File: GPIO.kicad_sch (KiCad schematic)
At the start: 0 parts

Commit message: Adde the sub sheet schematic for the GPIO and connected the Hierchal sheets together
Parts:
- added J10, J11, J14, J8: Conn_01x03_Pin, A_HDJ_Library:PinHeader_1x03_P2.54mm_Vertical, symbol Connector:Conn_01x03_Pin
- added J12, J13, J15, J16, J19, J7, J9: Conn_01x04_Pin, A_HDJ_Library:PinHeader_1x04_P2.54mm_Vertical, symbol Connector:Conn_01x04_Pin
- added U10, U11, U12, U17, U9: D3V3XA4B10LP, A_HDJ_Library:Diodes_UDFN-10_1.0x2.5mm_P0.5mm, symbol Power_Protection:D3V3XA4B10LP
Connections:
- new net: U17.3 (VSS), U17.8 (VSS)
- new net: U12.5, U12.6 (NC)
- new net: U10.5, U10.6 (NC)
- new net +3.3V: J13.1 (Pin_1), J13.2 (Pin_2), J13.3 (Pin_3), J13.4 (Pin_4), J14.1 (Pin_1), J14.2 (Pin_2), J14.3 (Pin_3), J19.1 (Pin_1), J19.2 (Pin_2), J19.3 (Pin_3), J19.4 (Pin_4)
- new net GND: J11.1 (Pin_1), J11.2 (Pin_2), J11.3 (Pin_3), J12.1 (Pin_1), J12.2 (Pin_2), J12.3 (Pin_3), J12.4 (Pin_4), J16.1 (Pin_1), J16.2 (Pin_2), J16.3 (Pin_3), J16.4 (Pin_4), U10.3 (VSS), U10.8 (VSS), U11.3 (VSS), U11.8 (VSS), U12.3 (VSS), U12.8 (VSS), U9.3 (VSS), U9.8 (VSS)
- new net GPP_D0: J15.1 (Pin_1), U17.1, U17.10 (NC)
- new net GPP_D1: J15.2 (Pin_2), U17.2, U17.9 (NC)
- new net GPP_D2: J15.3 (Pin_3), U17.4, U17.7 (NC)
- new net GPP_D3: J15.4 (Pin_4), U17.5, U17.6 (NC)
- new net I2C2_SCL: J9.1 (Pin_1), U11.1, U11.10 (NC)
- new net I2C2_SDA: J7.1 (Pin_1), U9.1, U9.10 (NC)
- new net I2C3_SCL: J9.2 (Pin_2), U11.2, U11.9 (NC)
- new net I2C3_SDA: J7.2 (Pin_2), U9.2, U9.9 (NC)
- new net I2C4_SCL: J9.3 (Pin_3), U11.4, U11.7 (NC)
- new net I2C4_SDA: J7.3 (Pin_3), U9.4, U9.7 (NC)
- new net I2C5_SCL: J9.4 (Pin_4), U11.5, U11.6 (NC)
- new net I2C5_SDA: J7.4 (Pin_4), U9.5, U9.6 (NC)
- new net SOC_UART0_RX: J8.1 (Pin_1), U10.1, U10.10 (NC)
- new net SOC_UART0_TX: J10.1 (Pin_1), U12.1, U12.10 (NC)
- new net SOC_UART1_RX: J8.2 (Pin_2), U10.2, U10.9 (NC)
- new net SOC_UART1_TX: J10.2 (Pin_2), U12.2, U12.9 (NC)
- new net SOC_UART2_RX: J8.3 (Pin_3), U10.4, U10.7 (NC)
- new net SOC_UART2_TX: J10.3 (Pin_3), U12.4, U12.7 (NC)

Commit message: finished the pciex4 implememntation
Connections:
- net GND: now also U17.3 (VSS), U17.8 (VSS)
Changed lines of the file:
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@@
+		)
+	)
+	(symbol
+		(lib_id "power:GND")
+		(at 243.84 87.63 0)
+		(unit 1)
+		(body_style 1)
+		(exclude_from_sim no)
+		(in_bom yes)
+		(on_board yes)
+		(in_pos_files yes)
+		(dnp no)
+		(fields_autoplaced yes)
+		(property "Reference" "#PWR0144"
+			(at 243.84 93.98 0)
+			(hide yes)
+			(show_name no)
+			(do_not_autoplace no)
+			(effects
+				(font
+					(size 1.27 1.27)
+				)
+			)
+		)
+		(property "Value" "GND"
+			(at 243.84 92.71 0)
+			(show_name no)
+			(do_not_autoplace no)
+			(effects
+				(font
+					(size 1.27 1.27)
+				)
+			)
+		)
+		(property "Footprint" ""
+			(at 243.84 87.63 0)
+			(hide yes)
+			(show_name no)
+			(do_not_autoplace no)
+			(effects
+				(font
+					(size 1.27 1.27)
+				)
+			)
+		)
+		(property "Datasheet" ""
+			(at 243.84 87.63 0)
+			(hide yes)
+			(show_name no)
+			(do_not_autoplace no)
+			(effects
+				(font
+					(size 1.27 1.27)
+				)
+			)
+		)
+		(property "Description" "Power symbol creates a global label with name \"GND\" , ground"
+			(at 243.84 87.63 0)
+			(hide yes)
+			(show_name no)
+			(do_not_autoplace no)
+			(effects
+				(font
+					(size 1.27 1.27)
+				)
+			)
+		)
+		(pin "1"
+		)
+		(instances
+			(project "Carrier_Board"
+				(path "/e768274e-12f3-4f83-96f6-abb7638e0bc1/f0c5bd9b-b5d7-485d-b3b5-c60eebcf14e3"
+					(reference "#PWR0144")
+					(unit 1)
+				)
+			)
 		)
 	)

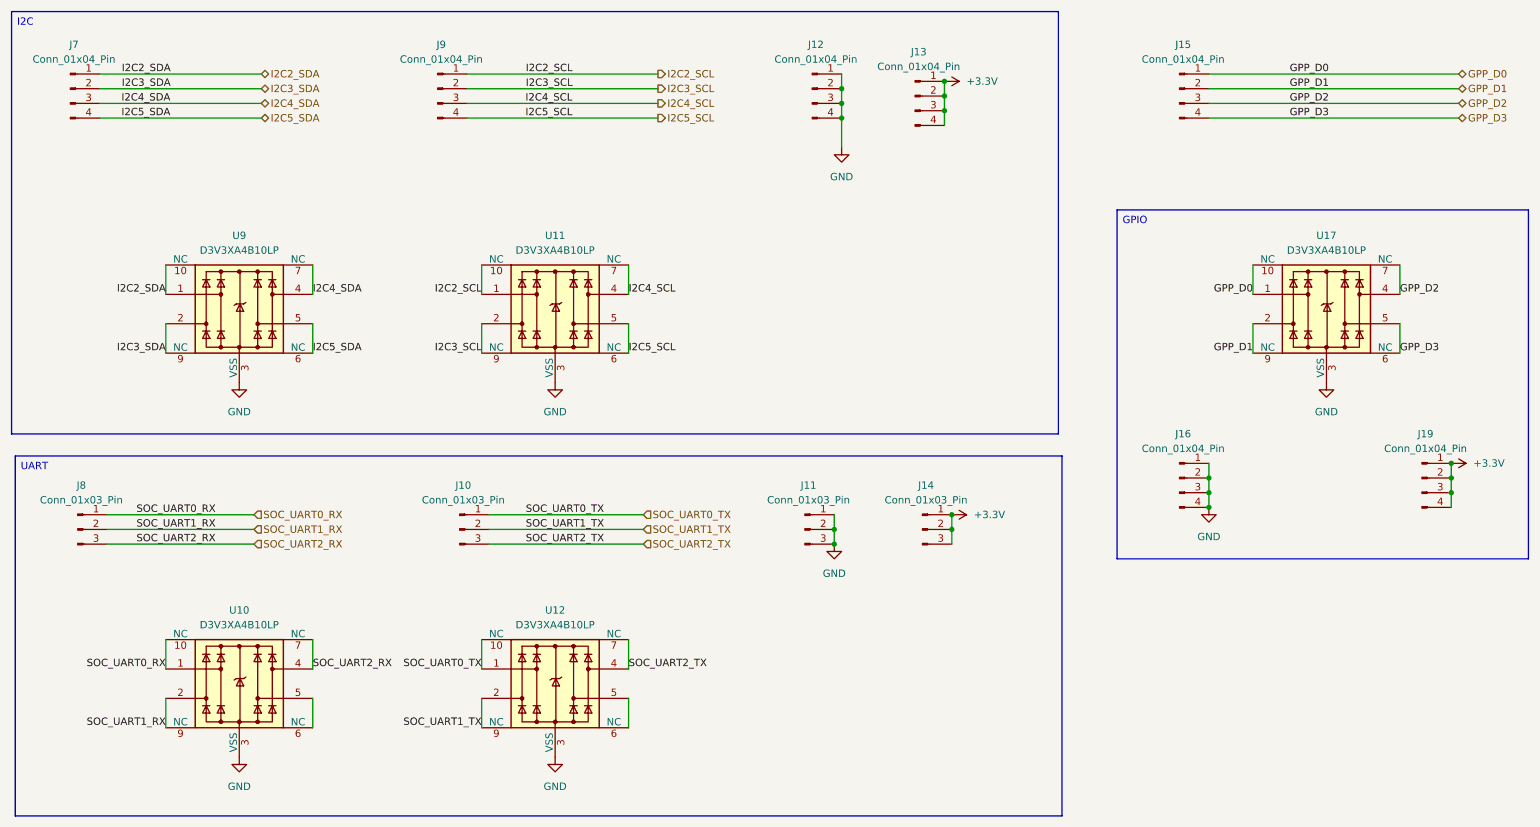
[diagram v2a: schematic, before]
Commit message: Fixed annotation errors duplicate designators on passive components R11 and J15 so that schematic could be imported into pcb. There might be some missing footprints... starting that investigation
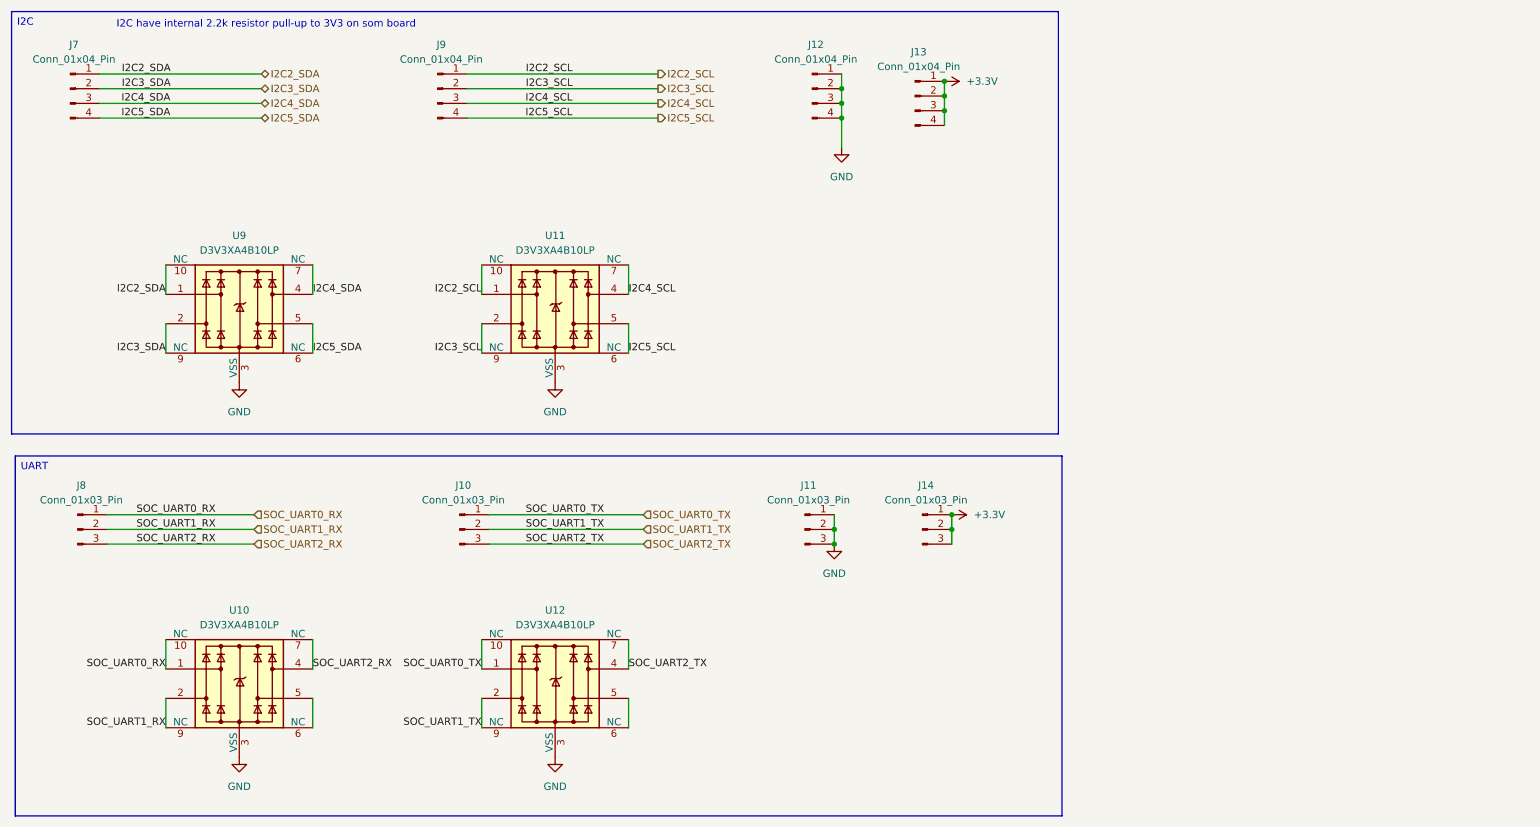
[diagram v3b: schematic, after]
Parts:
- removed J15, J16, J19: Conn_01x04_Pin, A_HDJ_Library:PinHeader_1x04_P2.54mm_Vertical, symbol Connector:Conn_01x04_Pin
- removed U17: D3V3XA4B10LP, A_HDJ_Library:Diodes_UDFN-10_1.0x2.5mm_P0.5mm, symbol Power_Protection:D3V3XA4B10LP
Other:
- note added: "I2C have internal 2.2k resistor pull-up to 3V3 on som board"

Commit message: Updated all the footprints into the pcb editor but all the designator numbers have changed... I have tp go back and fix each one
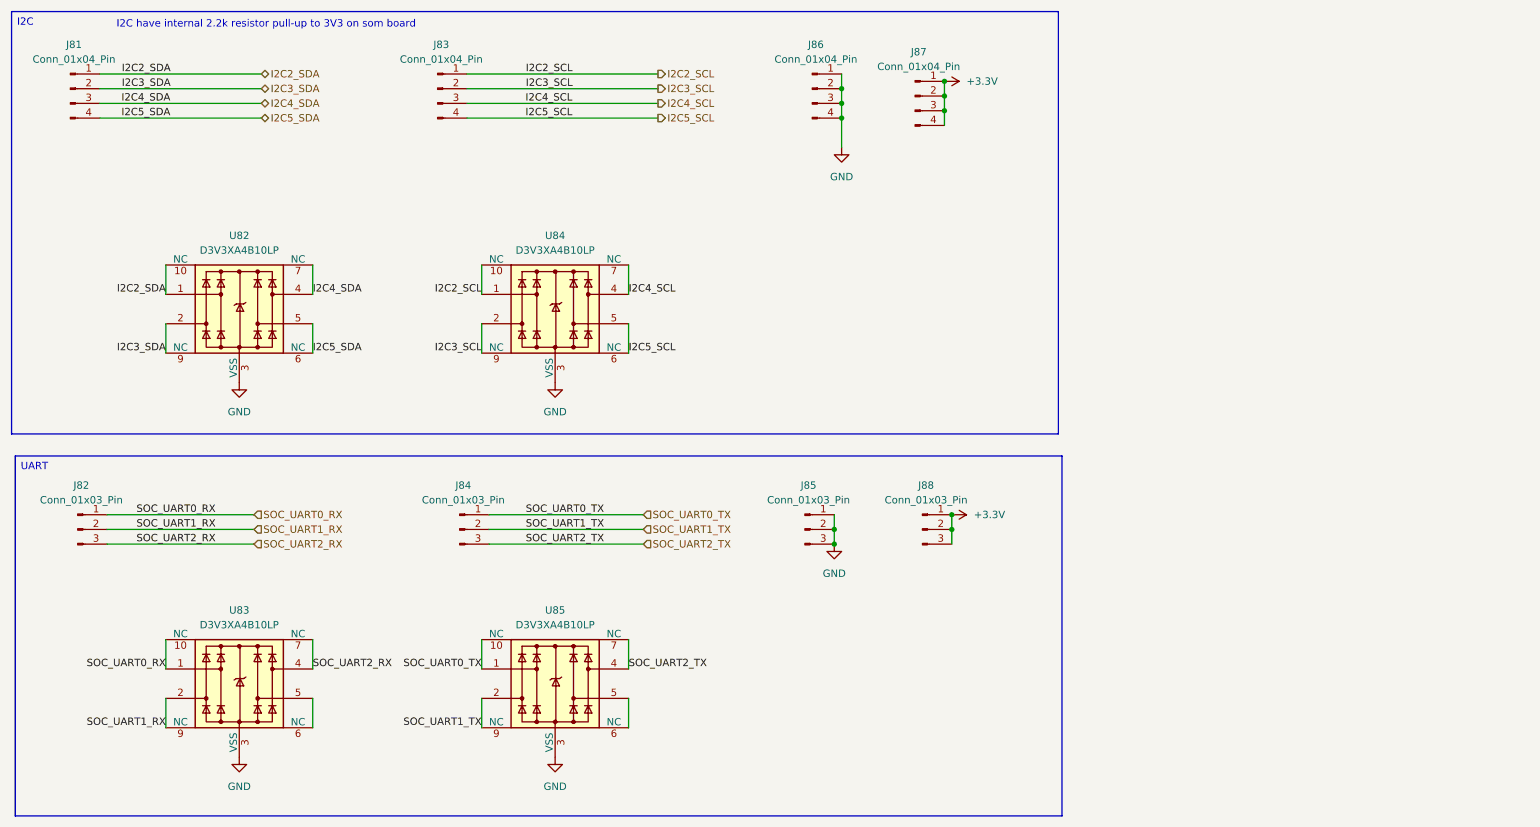
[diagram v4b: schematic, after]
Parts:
- renumbered J7 to J81, J8 to J82, J9 to J83, J10 to J84, J11 to J85, J12 to J86, J13 to J87, J14 to J88, U9 to U82, U10 to U83, U11 to U84, U12 to U85

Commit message: Designators in GPIO restored
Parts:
- renumbered J84 to J10, J85 to J11, J86 to J12, J87 to J13, J88 to J14, J81 to J7, J82 to J8, J83 to J9, U83 to U10, U84 to U11, U85 to U12, U82 to U9
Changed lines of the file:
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@@
 		(dnp no)
 		(fields_autoplaced yes)
-		(property "Reference" "J83"
+		(property "Reference" "J9"
 			(at 90.805 29.21 0)
 			(show_name no)
@@
 			(project "Carrier_Board"
 				(path "/e768274e-12f3-4f83-96f6-abb7638e0bc1/f0c5bd9b-b5d7-485d-b3b5-c60eebcf14e3"
-					(reference "J83")
+					(reference "J9")
 					(unit 1)
 				)
@@
 		(dnp no)
 		(fields_autoplaced yes)
-		(property "Reference" "J84"
+		(property "Reference" "J10"
 			(at 94.615 105.41 0)
 			(show_name no)
@@
 			(project "Carrier_Board"
 				(path "/e768274e-12f3-4f83-96f6-abb7638e0bc1/f0c5bd9b-b5d7-485d-b3b5-c60eebcf14e3"
-					(reference "J84")
+					(reference "J10")
 					(unit 1)
 				)
@@
 		(dnp no)
 		(fields_autoplaced yes)
-		(property "Reference" "U85"
+		(property "Reference" "U12"
 			(at 110.49 127 0)
 			(show_name no)
@@
 			(project "Carrier_Board"
 				(path "/e768274e-12f3-4f83-96f6-abb7638e0bc1/f0c5bd9b-b5d7-485d-b3b5-c60eebcf14e3"
-					(reference "U85")
+					(reference "U12")
 					(unit 1)
 				)
@@
 		(dnp no)
 		(fields_autoplaced yes)
-		(property "Reference" "U83"
+		(property "Reference" "U10"
 			(at 55.88 127 0)
 			(show_name no)
@@
 			(project "Carrier_Board"
 				(path "/e768274e-12f3-4f83-96f6-abb7638e0bc1/f0c5bd9b-b5d7-485d-b3b5-c60eebcf14e3"
-					(reference "U83")
+					(reference "U10")
 					(unit 1)
 				)
@@
 		(dnp no)
 		(fields_autoplaced yes)
-		(property "Reference" "U84"
+		(property "Reference" "U11"
 			(at 110.49 62.23 0)
 			(show_name no)
@@
 			(project "Carrier_Board"
 				(path "/e768274e-12f3-4f83-96f6-abb7638e0bc1/f0c5bd9b-b5d7-485d-b3b5-c60eebcf14e3"
-					(reference "U84")
+					(reference "U11")
 					(unit 1)
 				)
@@
 		(dnp no)
 		(fields_autoplaced yes)
-		(property "Reference" "J85"
+		(property "Reference" "J11"
 			(at 154.305 105.41 0)
 			(show_name no)
@@
 			(project "Carrier_Board"
 				(path "/e768274e-12f3-4f83-96f6-abb7638e0bc1/f0c5bd9b-b5d7-485d-b3b5-c60eebcf14e3"
-					(reference "J85")
+					(reference "J11")
 					(unit 1)
 				)
@@
 		(dnp no)
 		(fields_autoplaced yes)
-		(property "Reference" "J81"
+		(property "Reference" "J7"
 			(at 27.305 29.21 0)
 			(show_name no)
@@
 			(project "Carrier_Board"
 				(path "/e768274e-12f3-4f83-96f6-abb7638e0bc1/f0c5bd9b-b5d7-485d-b3b5-c60eebcf14e3"
-					(reference "J81")
+					(reference "J7")
 					(unit 1)
 				)
@@
 		(dnp no)
 		(fields_autoplaced yes)
-		(property "Reference" "J82"
+		(property "Reference" "J8"
 			(at 28.575 105.41 0)
 			(show_name no)
@@
 			(project "Carrier_Board"
 				(path "/e768274e-12f3-4f83-96f6-abb7638e0bc1/f0c5bd9b-b5d7-485d-b3b5-c60eebcf14e3"
-					(reference "J82")
+					(reference "J8")
 					(unit 1)
 				)
@@
 		(dnp no)
 		(fields_autoplaced yes)
-		(property "Reference" "J86"
+		(property "Reference" "J12"
 			(at 155.575 29.21 0)
 			(show_name no)
@@
 			(project "Carrier_Board"
 				(path "/e768274e-12f3-4f83-96f6-abb7638e0bc1/f0c5bd9b-b5d7-485d-b3b5-c60eebcf14e3"
-					(reference "J86")
+					(reference "J12")
 					(unit 1)
 				)
@@
 		(dnp no)
 		(fields_autoplaced yes)
-		(property "Reference" "J87"
+		(property "Reference" "J13"
 			(at 173.355 30.48 0)
 			(show_name no)
@@
 			(project "Carrier_Board"
 				(path "/e768274e-12f3-4f83-96f6-abb7638e0bc1/f0c5bd9b-b5d7-485d-b3b5-c60eebcf14e3"
-					(reference "J87")
+					(reference "J13")
 					(unit 1)
 				)
@@
 		(dnp no)
 		(fields_autoplaced yes)
-		(property "Reference" "U82"
+		(property "Reference" "U9"
 			(at 55.88 62.23 0)
 			(show_name no)
@@
 			(project "Carrier_Board"
 				(path "/e768274e-12f3-4f83-96f6-abb7638e0bc1/f0c5bd9b-b5d7-485d-b3b5-c60eebcf14e3"
-					(reference "U82")
+					(reference "U9")
 					(unit 1)
 				)
@@
 		(dnp no)
 		(fields_autoplaced yes)
-		(property "Reference" "J88"
+		(property "Reference" "J14"
 			(at 174.625 105.41 0)
 			(show_name no)
@@
 			(project "Carrier_Board"
 				(path "/e768274e-12f3-4f83-96f6-abb7638e0bc1/f0c5bd9b-b5d7-485d-b3b5-c60eebcf14e3"
-					(reference "J88")
+					(reference "J14")
 					(unit 1)
 				)
